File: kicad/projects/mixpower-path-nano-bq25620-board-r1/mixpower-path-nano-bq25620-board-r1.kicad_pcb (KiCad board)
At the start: 4 copper layers, 140 parts, among them J10 HAT, J11 DEBUG, J5 USB_C_Receptacle_USB2.0_16P, J6 BAT_HEADERS, J7 BATT, J8 DATA_CONN, J9 DATA_HEADER, Q4 Si1539CDL, Q5 AO3401A, Q6 DMN3032LFDBQ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

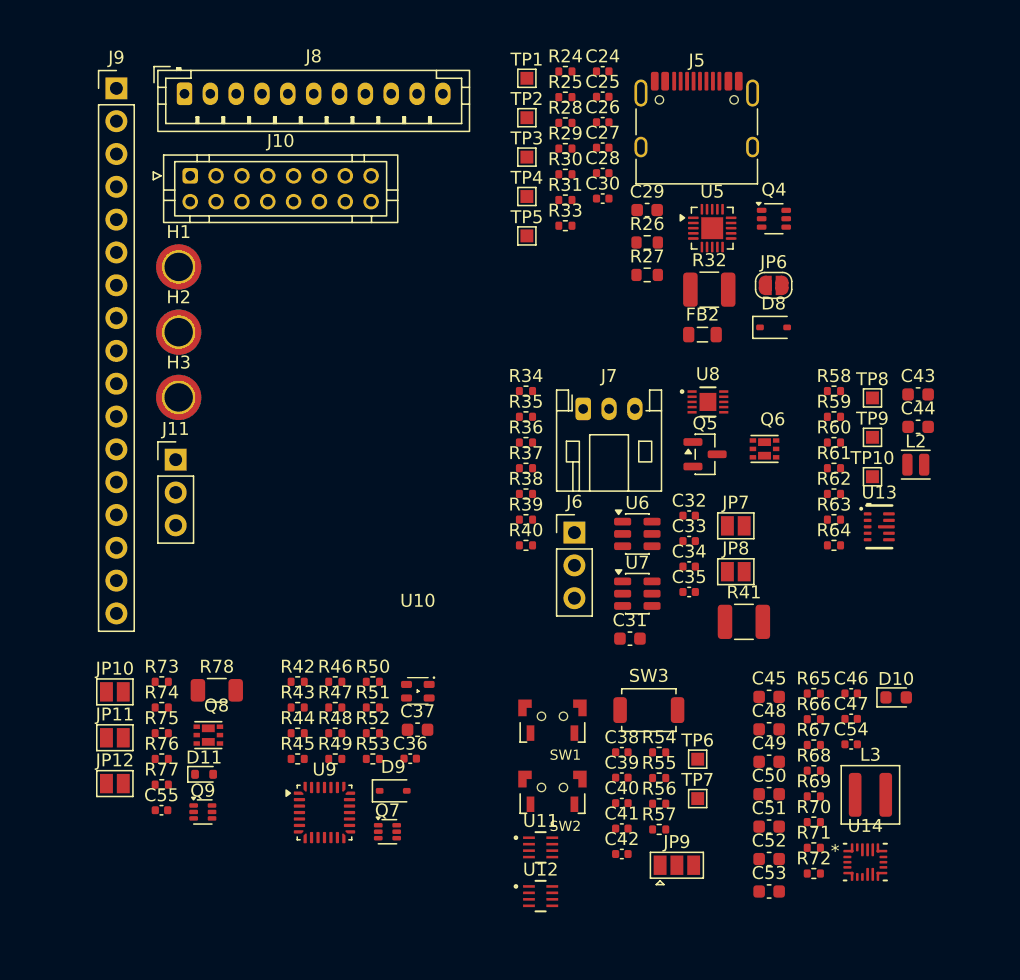
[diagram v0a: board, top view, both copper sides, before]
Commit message: feat: rework schematics and add proper calculations
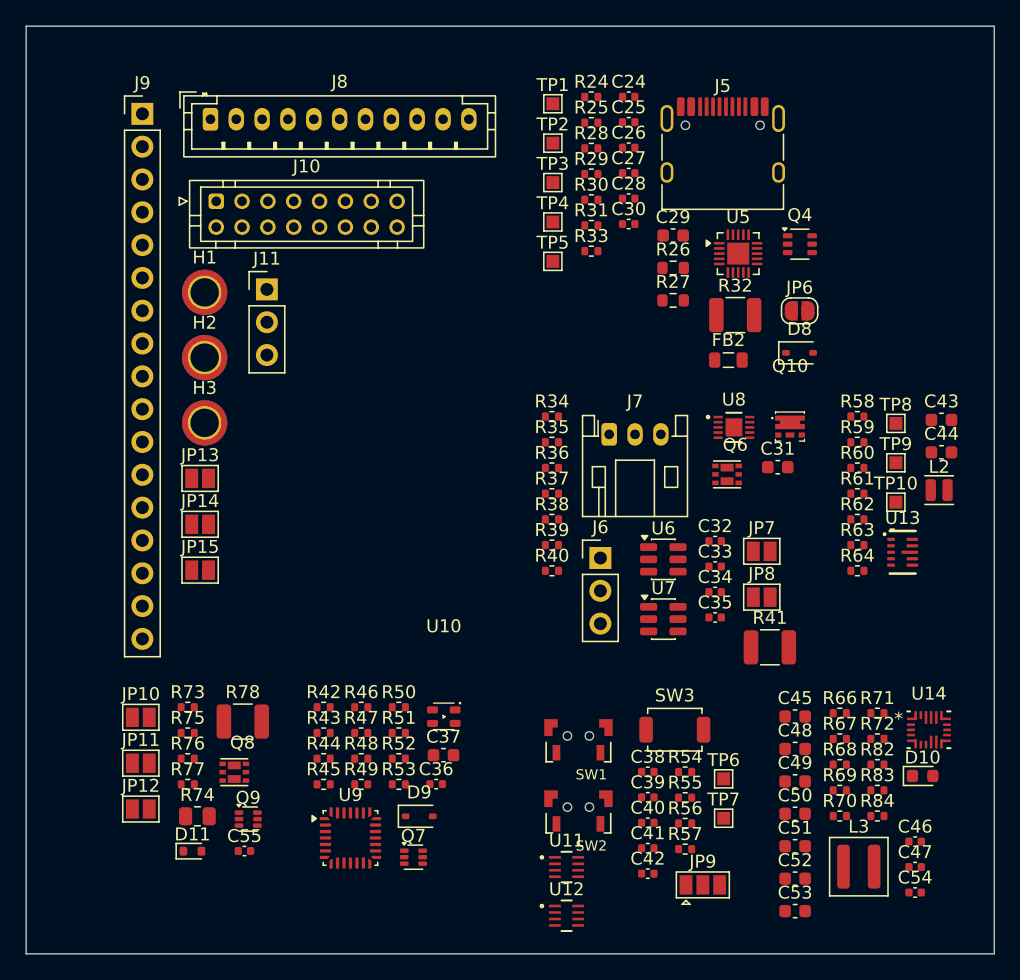
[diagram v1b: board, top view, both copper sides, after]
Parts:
- removed Q5: AO3401A, Package_TO_SOT_SMD:SOT-23
- removed R65: 1M, Resistor_SMD:R_0402_1005Metric
- added JP13: H1_SHIELD_TO_GND, Jumper:SolderJumper-2_P1.3mm_Open_Pad1.0x1.5mm, F.Cu at (123.8, 73.4)
- added JP14: H2_SHIELD_TO_GND, Jumper:SolderJumper-2_P1.3mm_Open_Pad1.0x1.5mm, F.Cu at (123.8, 76.9)
- added JP15: H3_SHIELD_TO_GND, Jumper:SolderJumper-2_P1.3mm_Open_Pad1.0x1.5mm, F.Cu at (123.8, 80.5)
- added Q10: NTLJS17D0P03P8Z, mixlib-vendor-onsemi:vendor-onsemi-483av, F.Cu at (169.5, 69.4)
- added R82: 0, Resistor_SMD:R_0402_1005Metric, F.Cu at (176.3, 95.5)
- added R83: 0, Resistor_SMD:R_0402_1005Metric, F.Cu at (176.3, 97.5)
- added R84: 0, Resistor_SMD:R_0402_1005Metric, F.Cu at (176.3, 99.5)
- R48, R49, R50: value 1.5k -> 1k
- R74: footprint Resistor_SMD:R_0402_1005Metric -> Resistor_SMD:R_0805_2012Metric
- R78: value 3.3k -> 1k; footprint Resistor_SMD:R_1206_3216Metric -> Resistor_SMD:R_1210_3225Metric
- SW3: value TS-A002 -> TS-1088
- TP1: value D+ -> D-
- TP2: value D- -> D+
- U7: value DW01A -> FS312F-G
- U9: value STM32G071G8UxN -> STM32G071G8U6N
- moved C31 17.5 mm to (168.6, 72.5)
- moved J11 15.0 mm to (129.0, 58.7)
- moved C54 12.5 mm to (179.2, 105.4)
- moved C46 12.5 mm to (179.2, 101.5)
- moved C47 12.5 mm to (179.2, 103.4)
- moved R71 11.5 mm to (176.3, 91.5)
- moved R72 11.5 mm to (176.3, 93.5)
- moved U14 11.4 mm to (180.3, 92.8)
- moved R74 8.86 mm to (123.6, 99.5)
- moved C55 7.16 mm to (127.3, 102.2)
- moved D10 6.42 mm to (179.8, 96.4)
- moved D11 6.02 mm to (123.2, 102.2)
- moved L3 5.63 mm to (174.8, 103.4)
- moved Q9 3.55 mm to (127.6, 99.7)
- moved Q6 3.51 mm to (164.6, 73.1)
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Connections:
- J10 pad 1: /output-headers/VOTG -> /output-headers/VBUS
- U10 pad 1: /output-headers/VSYS -> /output-headers/3V3
- U14 pad 4: /output-headers/D- -> Net-(U14-D-)
- U14 pad 5: /output-headers/D+ -> Net-(U14-D+)
- U14 pad 7: /output-headers/~{BTN} -> Net-(U14-~{QON})
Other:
- board outline added: 74.9 x 71.8 mm
